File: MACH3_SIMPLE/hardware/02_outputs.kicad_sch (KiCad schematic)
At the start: 15 parts, among them J1 LPT PORT 1, J10 X axis, J11 Y axis, J12 Z axis, J13 A axis, J14 B axis, J15 C axis, U1 74HC245, U2 74HC245

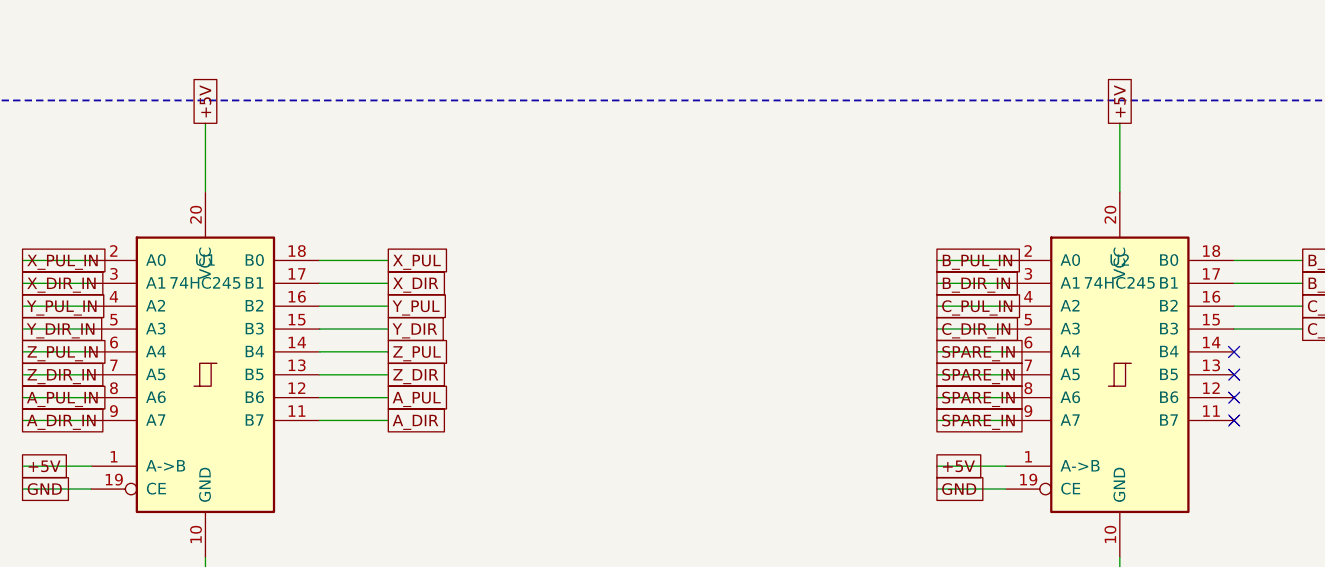
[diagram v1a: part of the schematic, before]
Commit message: MACH3-SIMPLE A1: design-review fixes and options
- Relay terminals labelled: RELAY A-F and NO/COM/NC per screw on the back
  silkscreen, RELAY A-F on the front (were on F.Fab only, not printed).
- R80-R85 4k7 -> 10k: 103 mW in a 100 mW 0603 on 24 V.
- Axis buffers fitted as 74AC245 (same pads) for opto-input drivers.
- J4 is 4-way: fused +24/0V for the sensors beside +24/0V in.
- C2 47 uF 50 V: 100 uF 50 V is not made in 6.3 x 7.7.
- Function labels (5V, 24V, SERIAL, A-F, 10V ADJ), test points GND/5V/24V
  and ACM/12V/AVI, dashed ISOLATED line round the VFD side, MCU heading
  moved beside the MCU.
- Buck switch node hand-drawn and locked: 14 mm top layer, no vias.
- F3 200 mA PTC on the handwheel +5V; 10 nF on MCU reset.
- Spare opto channel as VFD AUX output (port 2 pin 6); J5 is 6-way.
- autoroute.py keeps locked tracks through imports; route_one.py for a
  connection the router leaves open.

ERC 0, structural checks pass, DRC 0 errors / 0 unconnected / 0 parity,
barrier clean. Not built or powered.

Co-Authored-By: Claude Opus 5.5 <noreply@anthropic.com>
Claude-Session: https://claude.ai/code/session_01MByiLT2xCcbGPkgCYQy33q
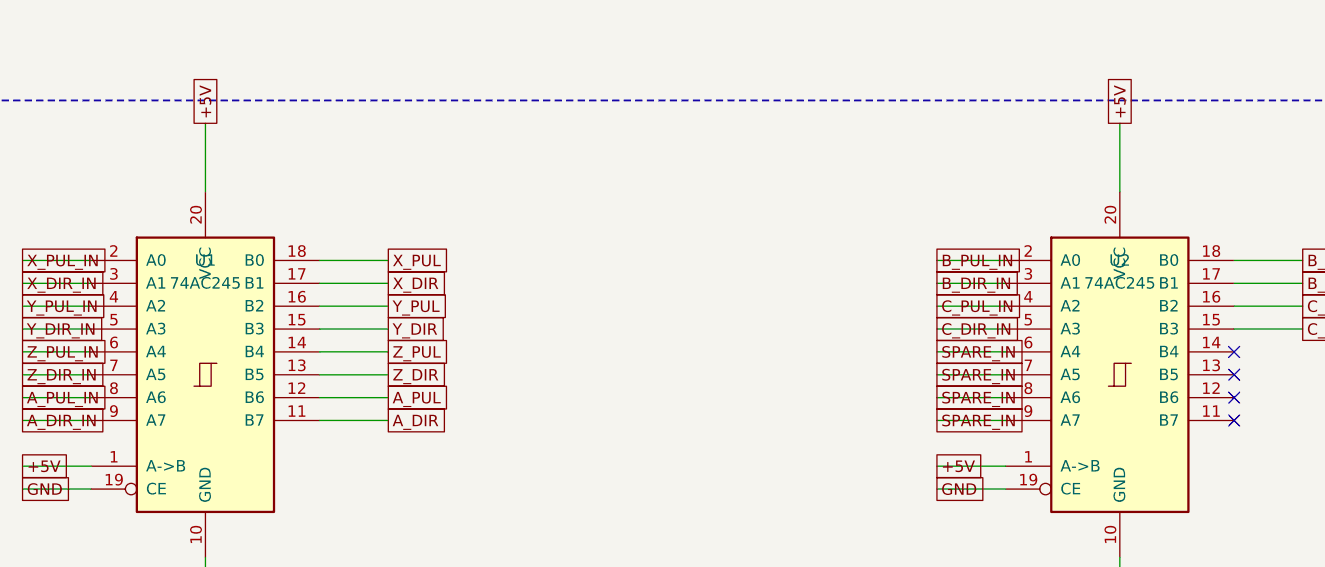
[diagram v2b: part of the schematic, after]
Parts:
- U1, U2: value 74HC245 -> 74AC245
